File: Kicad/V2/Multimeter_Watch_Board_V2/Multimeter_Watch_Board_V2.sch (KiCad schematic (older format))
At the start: 59 parts, among them J1 S3B-PH-K-S(LF)(SN), J2 S3B-PH-K-S(LF)(SN), J3 S3B-PH-K-S(LF)(SN), J6 51281-1294, J7 Conn_01x11_Female, J8 Conn_01x11_Female, Q1 A03400A N-MOS, U1 PCF85163-SO08, U2 AD8592, Y1 32kHz

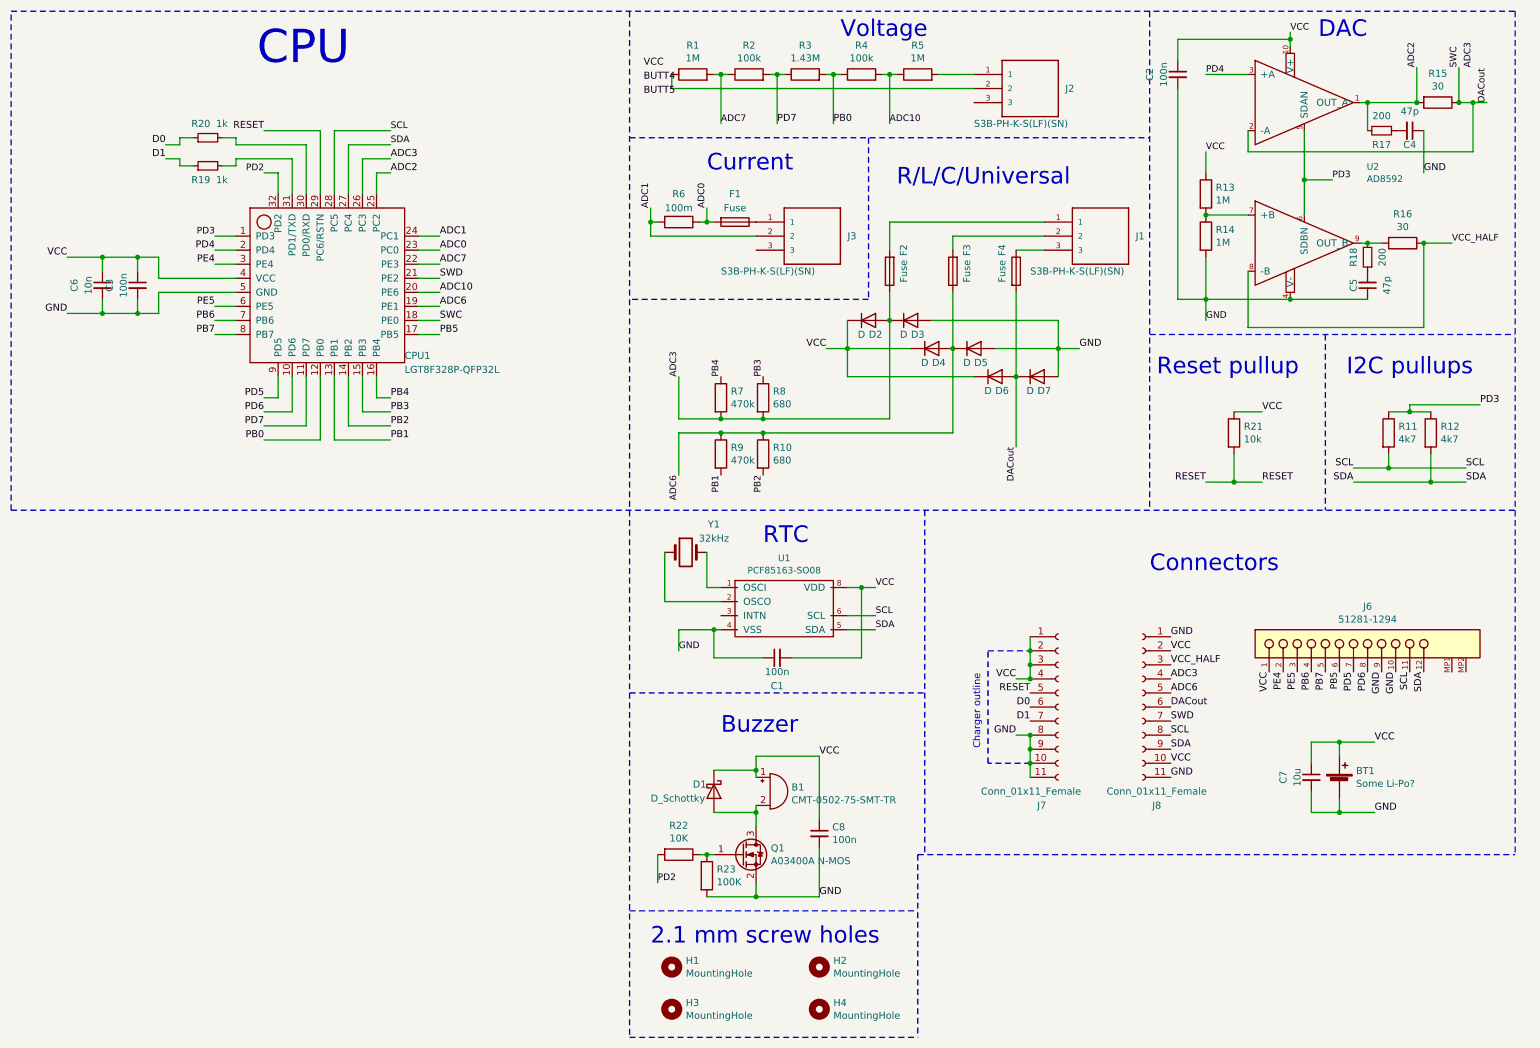
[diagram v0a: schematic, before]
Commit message: Revert "add rlc tester protection to schematic"
This reverts commit df46bc8d5560e11f4e55d6f466ca62c966db9fe4.
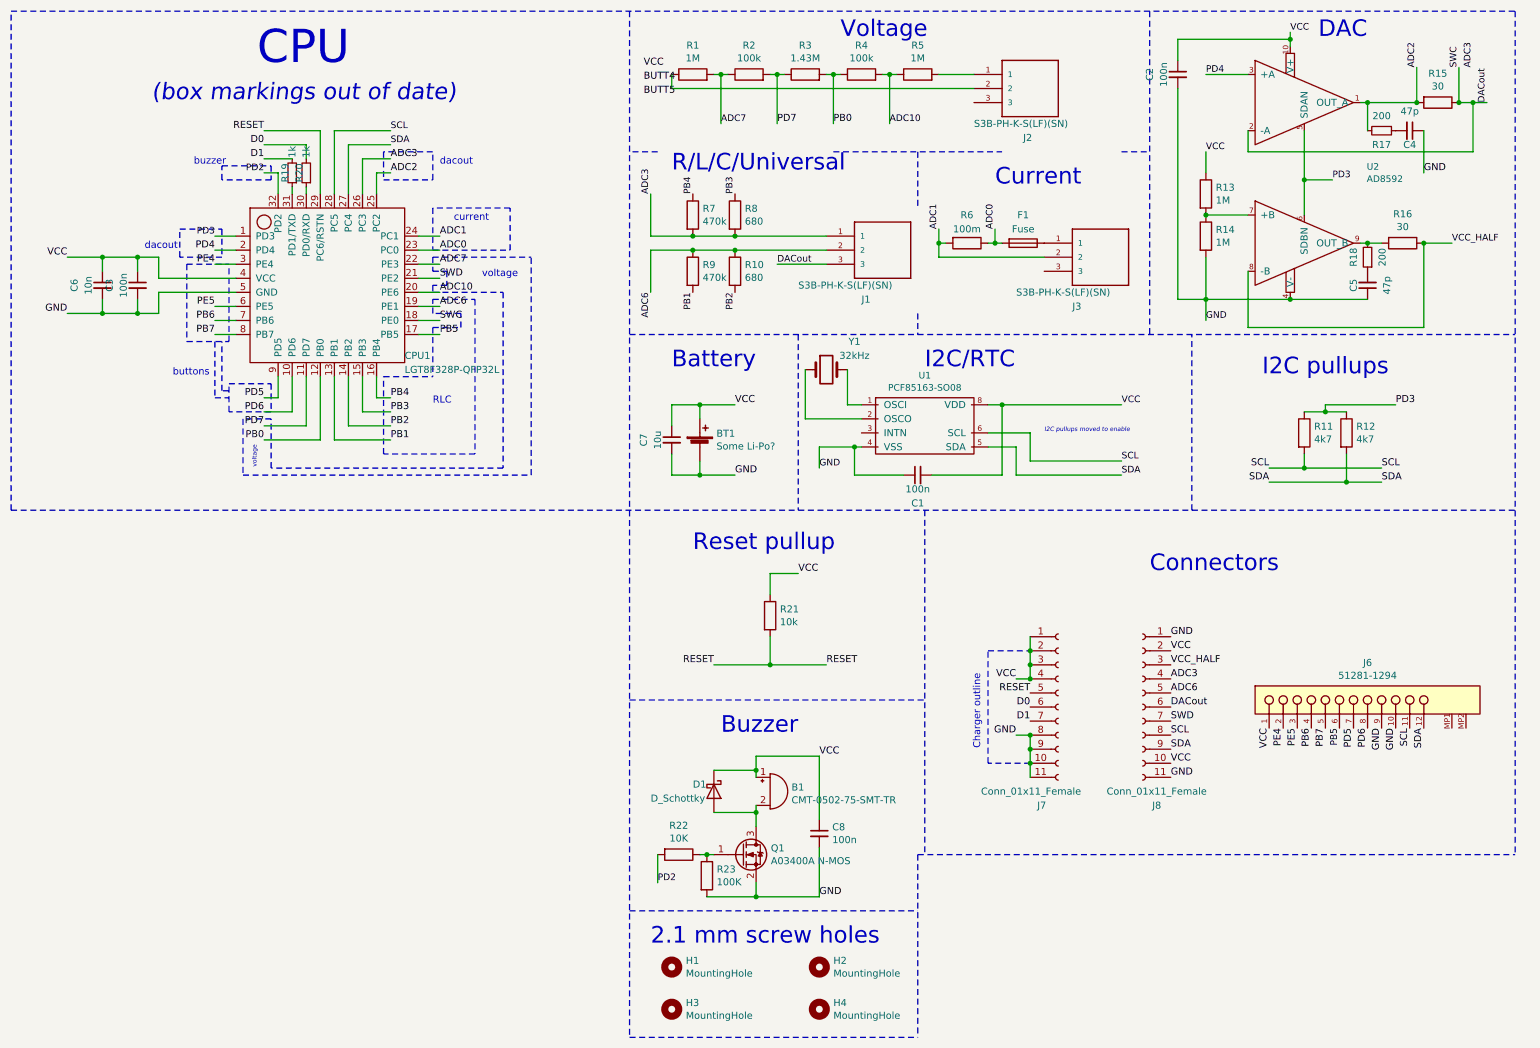
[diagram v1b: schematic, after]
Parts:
- removed D2, D3, D4, D5, D6, D7: D, Multimeter_Watch_Custom_Footprints:1408D, symbol Device:D
- removed F2, F3, F4: Fuse, Fuse:Fuse_0805_2012Metric_Pad1.15x1.40mm_HandSolder, symbol Device:Fuse
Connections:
- net ADC3: now also J1.1
- net ADC6: now also J1.2
- net D0: now also R20.2; no longer R20.1
- net D1: now also R19.2; no longer R19.1
- net DACout: now also J1.3
- net at CPU1.30 (PD0/RXD): now also R20.1; no longer R20.2
- net at CPU1.31 (PD1/TXD): now also R19.1; no longer R19.2
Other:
- note added: "(box markings out of date)"
- note added: "Battery"
- note added: "I2C pullups moved to enable"
- note added: "I2C/RTC\n"
- note added: "RLC\n"
- note added: "buttons\n"
- note added: "buzzer"
- note added: "current\n"
- note added: "dacout"
- note added: "dacout\n"
- note added: "voltage\n"
- note removed: "RTC\n"
- moved on the sheet: BT1, C1, C7, F1, J1, J3, J6, R10, R11, R12, R19, R20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
